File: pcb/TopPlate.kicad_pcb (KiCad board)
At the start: 2 copper layers, 138.2 x 110 mm, 6 parts

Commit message: update kicad project pcbs
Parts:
- removed REF**: boring_sofle_text, BoringSofle:boring_sofle_text
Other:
- board size 138.2 x 110 mm -> 136 x 110 mm

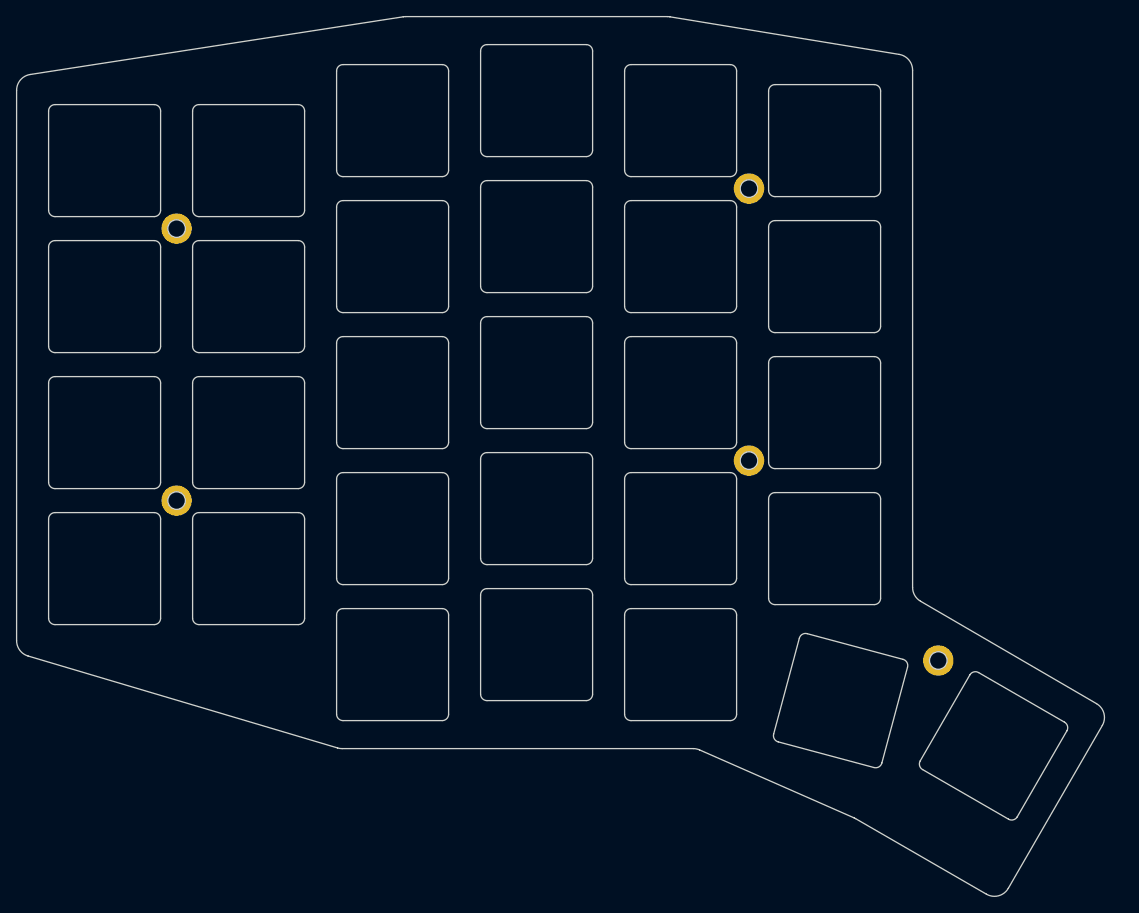
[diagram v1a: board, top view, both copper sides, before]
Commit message: shift encoder position and rotation, redesign top plate
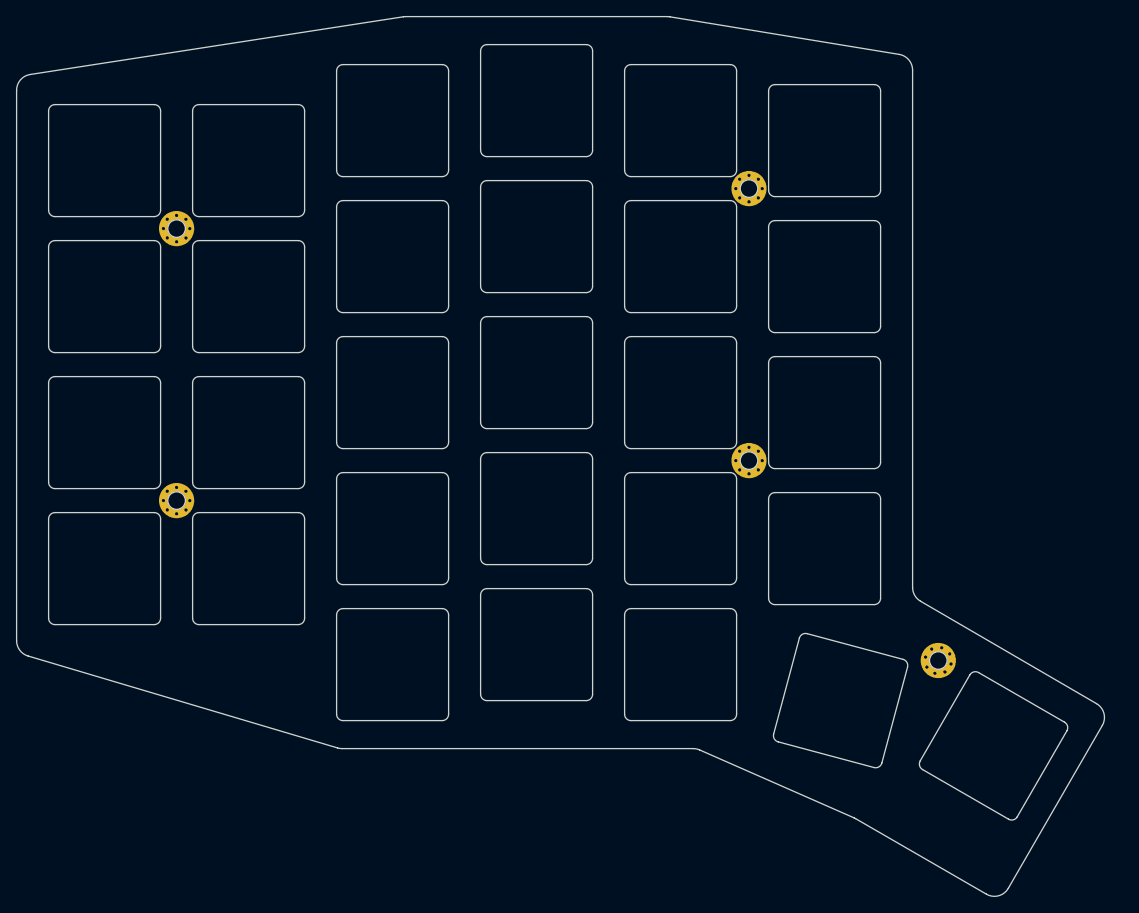
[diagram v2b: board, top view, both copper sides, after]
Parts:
- removed H1, H2, H3, H4, H5: , ceoloide:mounting_hole_plated
- added REF**: boring_sofle_text, BoringSofle:boring_sofle_text, F.Cu at (167.8, 177.8)
- added _1: , MountingHole_2.2mm_M2_Pad_Via, F.Cu at (159.0, 120.5)
- added _2: , MountingHole_2.2mm_M2_Pad_Via, F.Cu at (230.6, 115.5)
- added _3: , MountingHole_2.2mm_M2_Pad_Via, F.Cu at (159.0, 154.5)
- added _4: , MountingHole_2.2mm_M2_Pad_Via, F.Cu at (230.6, 149.5)
- added _5: , MountingHole_2.2mm_M2_Pad_Via, F.Cu at (254.2, 174.5)
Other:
- board text added: "JLCJLCJLCJLC"
